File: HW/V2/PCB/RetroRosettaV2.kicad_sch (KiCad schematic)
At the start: 8 parts, among them U1 ESP32-DevKitC

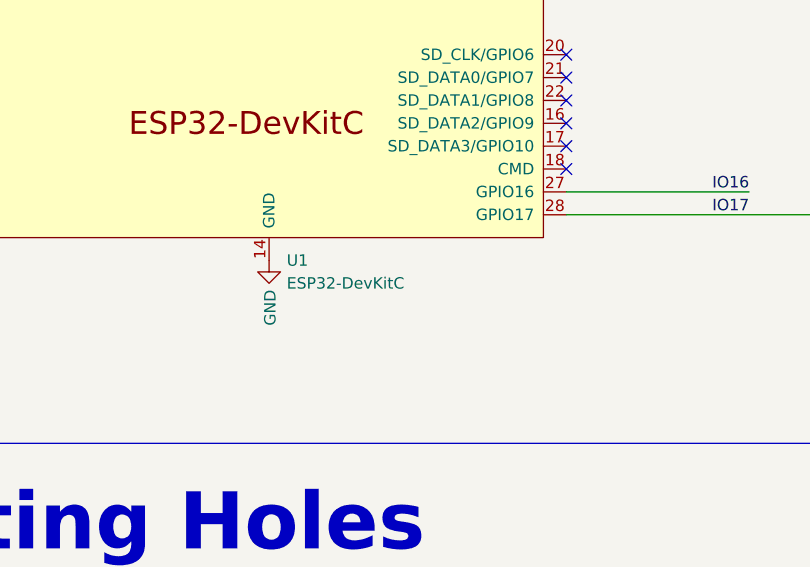
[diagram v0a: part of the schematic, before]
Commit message: Migrate documentation for V2
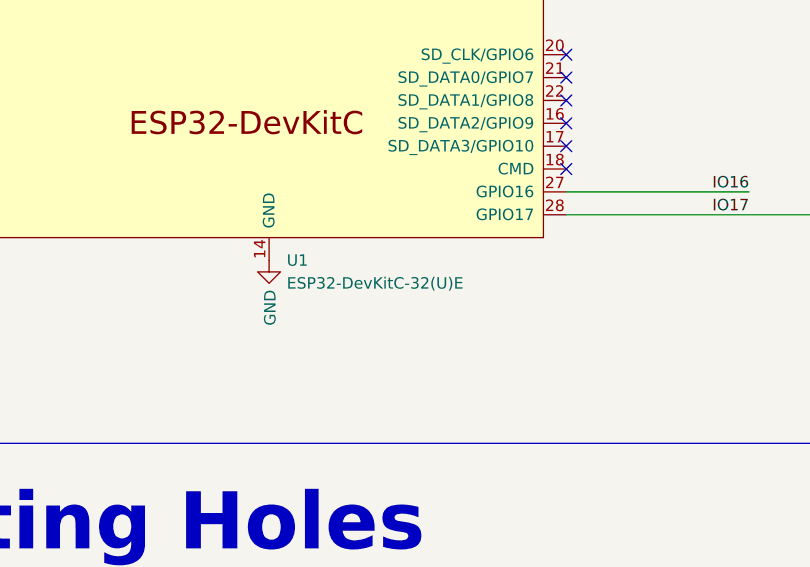
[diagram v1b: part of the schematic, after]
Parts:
- U1: value ESP32-DevKitC -> ESP32-DevKitC-32(U)E; DigiKey Part Number DNP -> 1965-ESP32-DEVKITC-32E-ND; Manufacturer_Part_Number DNP -> ESP32-DEVKITC-32E
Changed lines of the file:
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@@
       (effects (font (size 1.27 1.27)) (justify left))
     )
-    (property "Value" "ESP32-DevKitC" (at 76.8859 120.65 0)
+    (property "Value" "ESP32-DevKitC-32(U)E" (at 76.8859 120.65 0)
       (effects (font (size 1.27 1.27)) (justify left))
     )
@@
       (effects (font (size 1.27 1.27)) hide)
     )
-    (property "DigiKey Part Number" "DNP" (at 74.93 82.55 0)
+    (property "DigiKey Part Number" "1965-ESP32-DEVKITC-32E-ND" (at 74.93 82.55 0)
       (effects (font (size 1.27 1.27)) hide)
     )
-    (property "Manufacturer_Part_Number" "DNP" (at 74.93 82.55 0)
+    (property "Manufacturer_Part_Number" "ESP32-DEVKITC-32E" (at 74.93 82.55 0)
       (effects (font (size 1.27 1.27)) hide)
     )
